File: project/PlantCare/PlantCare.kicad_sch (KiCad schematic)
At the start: 41 parts, among them J1 TFT_0.96_13, J2 TTL-connect-pin4, J3 usbc, J4 Conn_01x02_Female, J5 Conn_01x01_Female, Q1 S8050, Q2 S8050, Q3 S8050, Q4 Q_NMOS_GSD, SW1 SW_DPDT_x2, SW2 SW_Push, SW3 SW_Push, U1 AMS1117-3.3, U2 ESP-12E, U3 CH340C

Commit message: update
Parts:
- removed C2, C3, C5: 10uf, Capacitor_SMD:C_0402_1005Metric, symbol Device:C
- removed C6, C7: 100nf, Capacitor_SMD:C_0402_1005Metric, symbol Device:C
- removed D2: B120-E3, Diode_SMD:D_SOD-123, symbol Diode:B120-E3
- removed J2: TTL-connect-pin4, Connector_PinHeader_1.27mm:PinHeader_1x04_P1.27mm_Vertical, symbol My-lib:TTL-connect-pin4
- removed J3: usbc, Connector_USB:USB_C_Receptacle_HRO_TYPE-C-31-M-12, symbol Connector:USB_C_Receptacle_USB2.0
- removed J5: Conn_01x01_Female, Connector_PinHeader_2.54mm:PinHeader_1x01_P2.54mm_Vertical, symbol Connector:Conn_01x01_Female
- removed Q2, Q3: S8050, Package_TO_SOT_SMD:TSOT-23, symbol Device:Q_NPN_BEC
- removed R11, R12: 470, Resistor_SMD:R_0402_1005Metric, symbol Device:R
- removed R14, R15: 12K, Resistor_SMD:R_0402_1005Metric, symbol Device:R
- removed SW1: SW_DPDT_x2, Button_Switch_SMD:SW_SPDT_PCM12, symbol Switch:SW_DPDT_x2
- removed U1: AMS1117-3.3, Package_TO_SOT_SMD:SOT-223-3_TabPin2, symbol Regulator_Linear:AMS1117-3.3
- removed U3: CH340C, lc_lib:SOP-16_150MIL, symbol Interface_USB:CH340C
- added D? (x2): led-white, LED_SMD:LED_0402_1005Metric, symbol Device:LED
- added J? (x2): Conn_01x02_Female, symbol Connector:Conn_01x02_Female
- added J?: TTL-connect-pin4, symbol My-lib:TTL-connect-pin4
- added Q?: Q_NMOS_GSD, Package_TO_SOT_SMD:TSOT-23, symbol Device:Q_NMOS_GSD
- added R? (x2): 12K, Resistor_SMD:R_0402_1005Metric, symbol Device:R
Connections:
- net +BATT: now also J?.2 (Pin_2), J?.2 (Pin_2), R?.1, R?.1
- net EN: now also J?.5 (RST)
- net GND: now also J?.1 (GND), Q?.2 (S)
- net GPIO0: now also J?.2 (GPIO0)
- net GPIO12: now also Q?.1 (G)
- net RXD: now also J?.3 (RXD)
- net TXD: now also J?.4 (TXD)
- net control: now also D?.1 (K), J?.1 (Pin_1)
- new net: D?.2 (A), R?.2 (x2)
- new net control1: D?.1 (K), J?.1 (Pin_1), Q?.3 (D)
- no-connect marks 19 -> 9
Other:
- added sheet POWER (PlantCarer-Power.kicad_sch)
- note added: "MOTO"
- note added: "v1.1 改动 1. AMS1117留4个位置，并联，可以不用。 2. 烧录器，LED位置可以不用。 3. 按键 led 电路可以放在背板不用放置元件 4. 被控制电路接LED显示开关状态 5. 去掉usb-uart 6. 增加一路控制 7. 烧录接口改成5pin 8. 连接电池，电机，改成接线柱连接"
- moved on the sheet: Q4

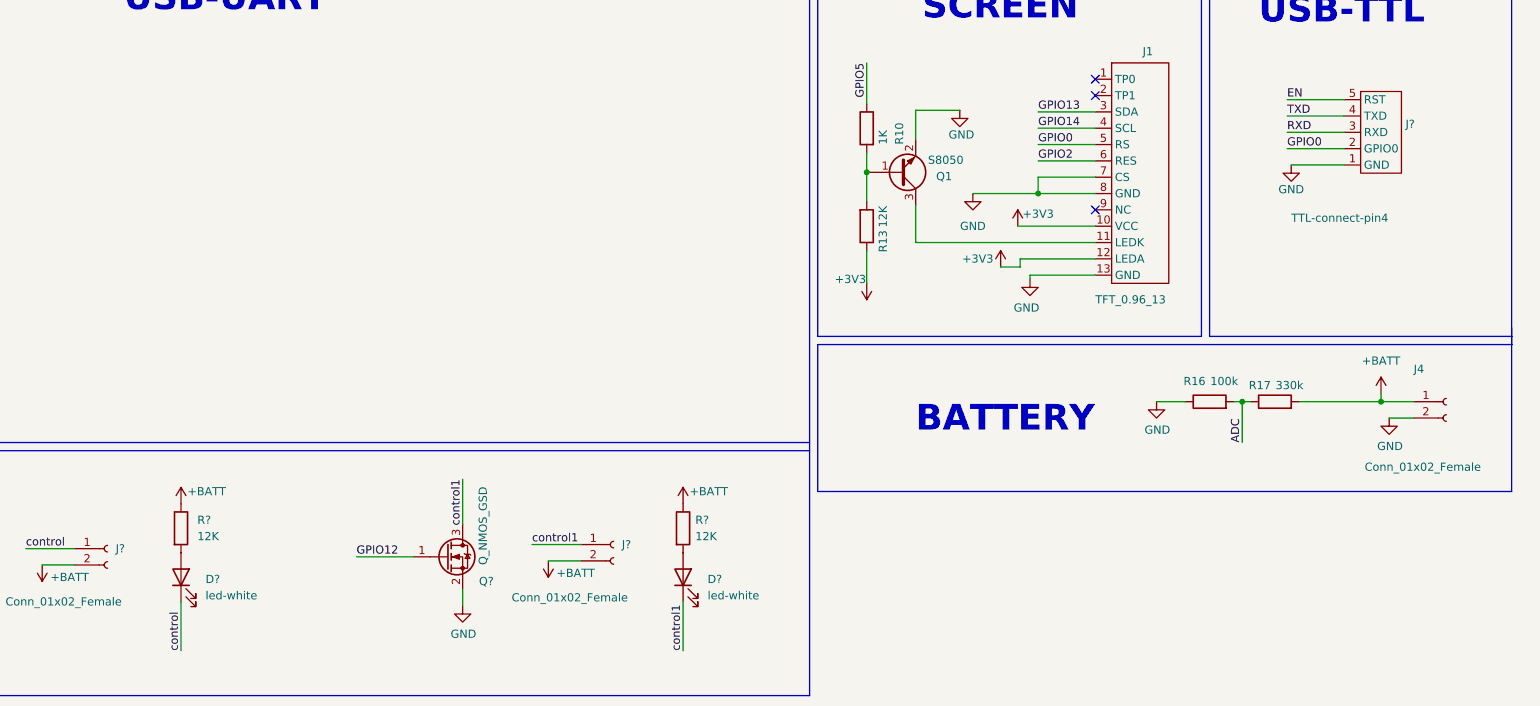
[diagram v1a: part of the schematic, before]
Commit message: update plant carer 1.2
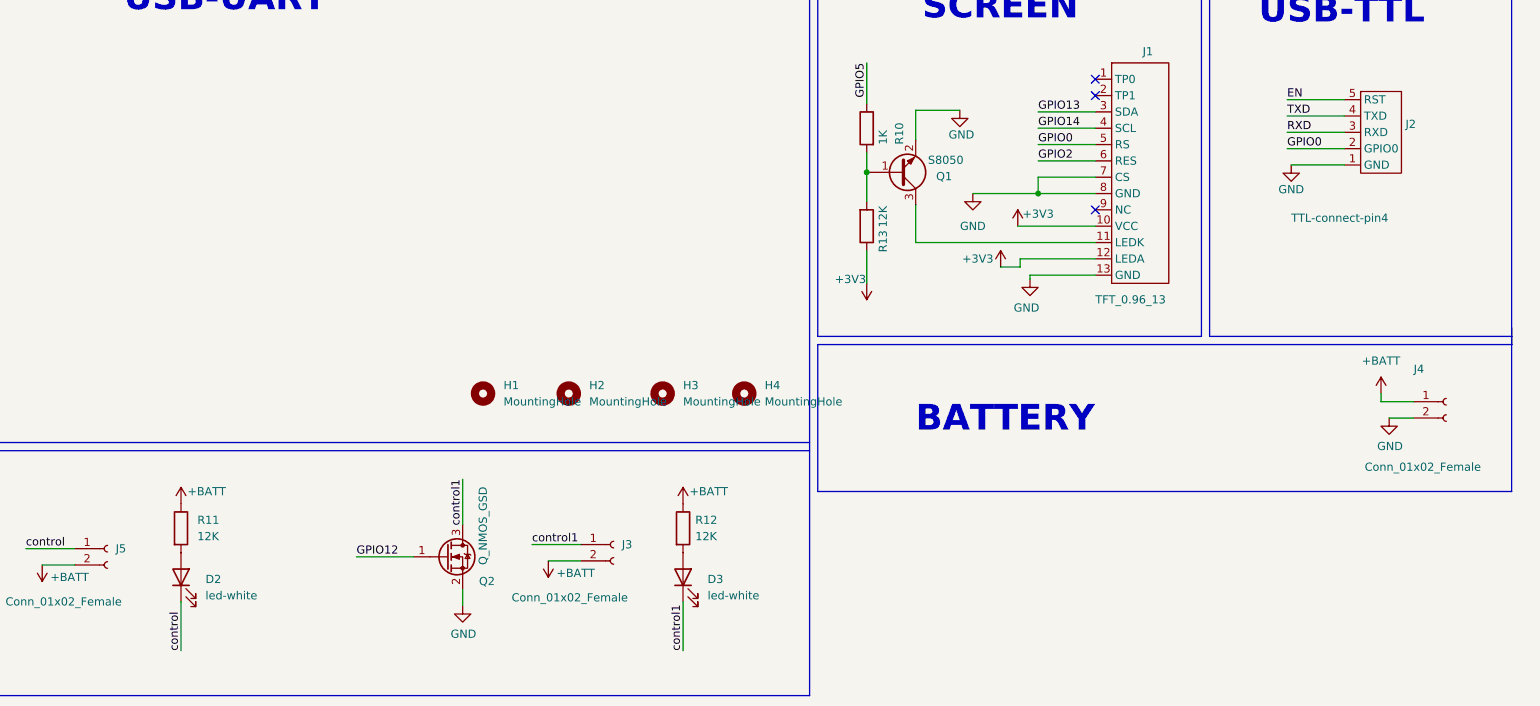
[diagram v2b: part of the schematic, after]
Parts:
- removed R16: 100k, Resistor_SMD:R_0402_1005Metric, symbol Device:R
- removed R17: 330k, Resistor_SMD:R_0402_1005Metric, symbol Device:R
- added H1, H2, H3, H4: MountingHole, MountingHole:MountingHole_2.5mm_Pad_Via, symbol Mechanical:MountingHole
- J2: renamed from J?; footprint (none) -> Connector_PinHeader_2.00mm:PinHeader_1x05_P2.00mm_Vertical
- J3, J5: renamed from J?; footprint (none) -> My-lib-footprints:Connect_push_5mm
- J4: footprint Connector_PinHeader_2.54mm:PinHeader_1x02_P2.54mm_Vertical -> My-lib-footprints:Connect_push_5mm
- gave numbers to parts that had none: 5
